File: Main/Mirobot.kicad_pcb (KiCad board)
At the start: 2 copper layers, 110 x 31.2 mm, 20 parts, among them IC1 ARDUINO_PRO_MINI, M1 ESP8266-ESP-07, P3 RIGHT_STEPPER, P4 LEFT_STEPPER, SW1 POWER_SWITCH, SW2 LEFT_BUMP, SW3 RIGHT_BUMP, U2 ULN2803A

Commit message: Updated for version 2.0f
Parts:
- added P1: CONN_01X02, Mirobot:2-PIN-EDGE-CONN, B.Cu at (201.8, 105.9)
- LINE1: moved to B.Cu
- M1: value ESP8266-ESP-07 -> ESP8266-ESP-12
- R1, R2, R3: footprint Resistors_SMD:R_0603_HandSoldering -> Mirobot:R_0603_HandSoldering_Universal_TH
- moved R2 3.30 mm to (161.8, 129.7), turned to 90 degrees
- moved PEN1 2.54 mm to (132.5, 130.6), turned to 270 degrees
- moved R3 2.16 mm to (170.8, 120.8)
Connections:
- M1 pad 11: (no net) -> Net-(M1-Pad11)
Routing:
- net Net-(M1-Pad11): track 0.00 -> 32.7 mm, vias 0 -> 2
- net GND: track 40.0 -> 63.7 mm, vias 9 -> 17
- net Net-(M1-Pad10): track 3.54 -> 8.30 mm
- net Net-(IC1-Pad17): track 41.8 -> 44.9 mm
- net +3V3: track 96.1 -> 93.7 mm
- net Net-(IC1-Pad18): track 45.7 -> 47.7 mm
- net Net-(IC1-Pad16): track 38.1 -> 40.0 mm, vias 2 -> 1
- net Net-(M1-Pad1): track 11.4 -> 12.5 mm
- net Net-(IC1-Pad12): track 55.3 -> 55.9 mm
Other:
- board text added: "POWER"
- board text added: "v2.0f"
- board text removed: "v2.0d"

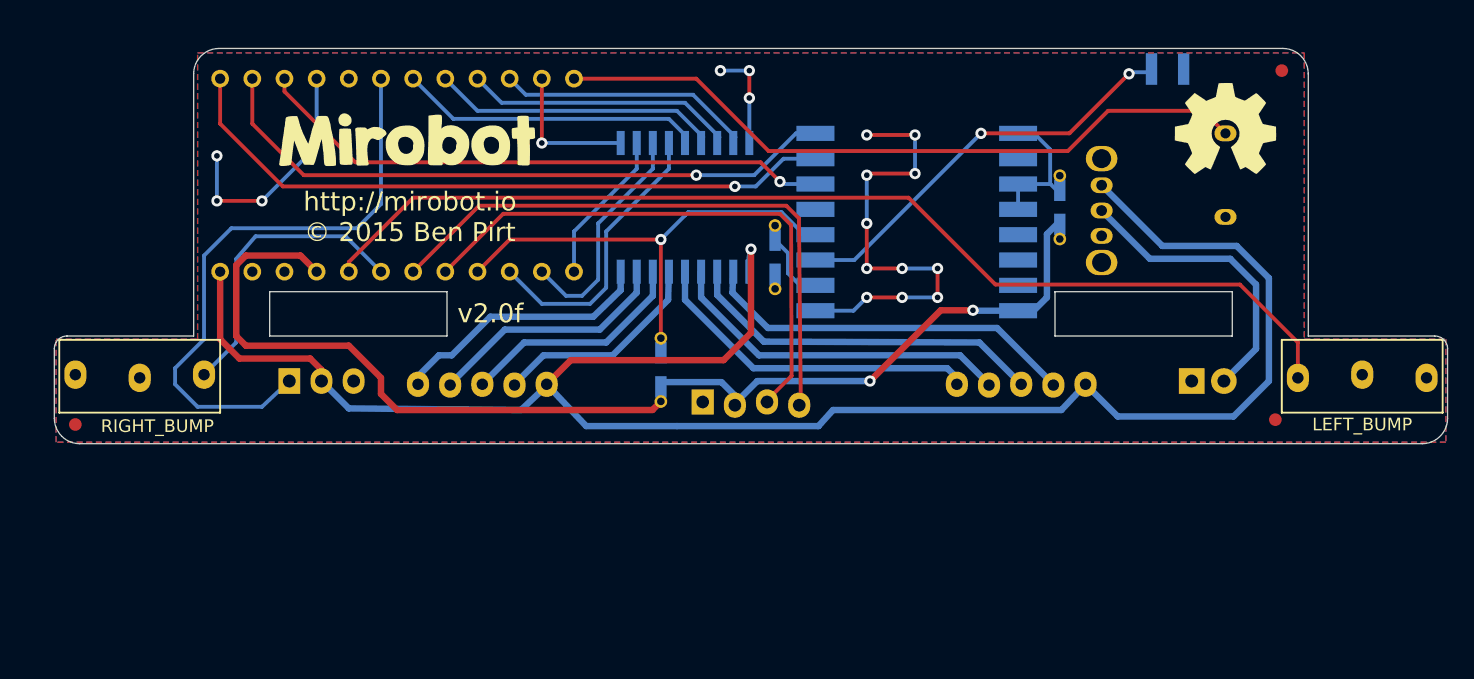
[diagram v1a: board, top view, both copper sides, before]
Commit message: Use a different pin for bringing GPIO0 out
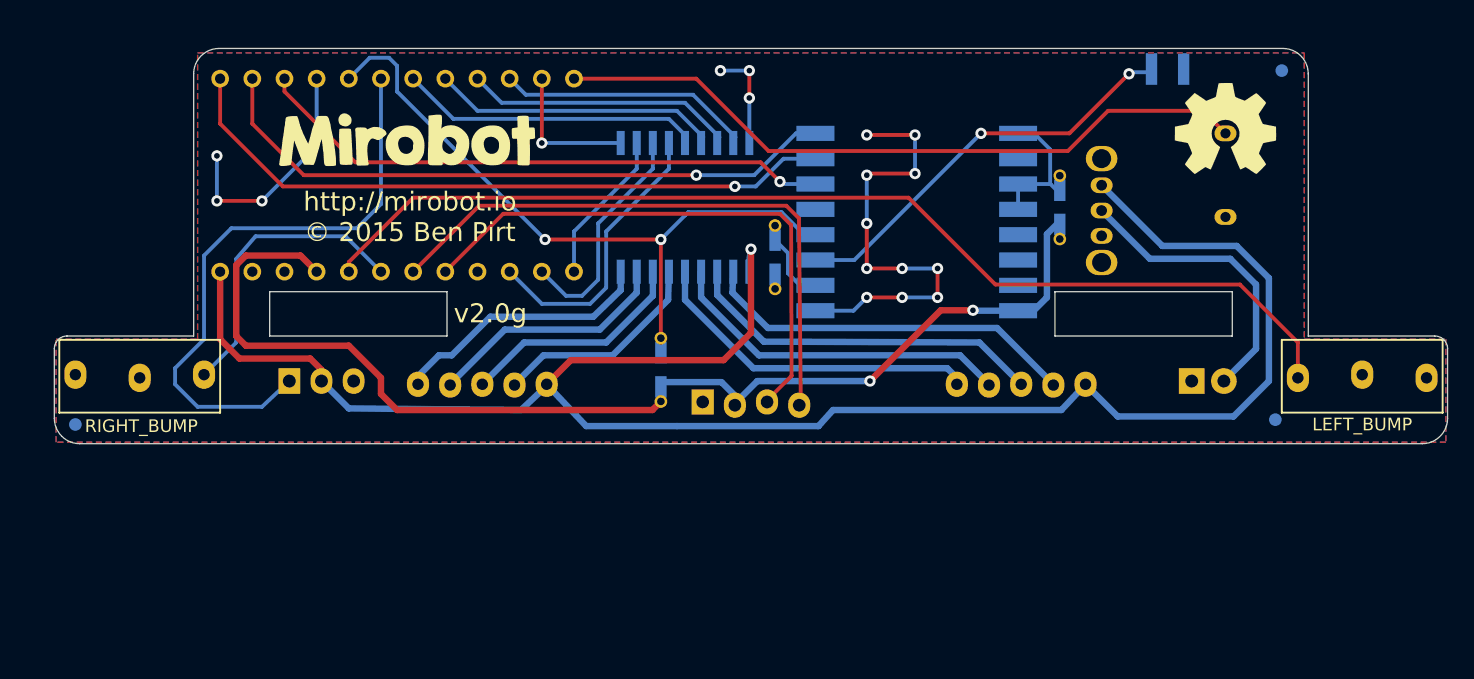
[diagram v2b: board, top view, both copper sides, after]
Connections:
- IC1 pad 16: Net-(IC1-Pad16) -> (no net)
- IC1 pad 5: (no net) -> Net-(IC1-Pad5)
- M1 pad 12: Net-(IC1-Pad16) -> Net-(IC1-Pad5)
- R2 pad 2: Net-(IC1-Pad16) -> Net-(IC1-Pad5)
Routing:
- net Net-(IC1-Pad5): track 0.00 -> 56.9 mm, vias 0 -> 2
- net Net-(IC1-Pad16): track 40.0 -> 0.00 mm, vias 1 -> 0
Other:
- board text added: "v2.0g"
- board text removed: "v2.0f"
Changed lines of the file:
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@@
     (thickness 1.6)
     (drawings 37)
-    (tracks 271)
+    (tracks 276)
     (zones 0)
     (modules 21)
@@
     (mod_text_size 1 1)
     (mod_text_width 0.15)
-    (pad_size 0.9 2.5)
+    (pad_size 1 1)
     (pad_drill 0)
     (pad_to_mask_clearance 0)
@@
   (net 30 "Net-(M1-Pad1)")
   (net 31 "Net-(M1-Pad10)")
-  (net 32 "Net-(IC1-Pad16)")
-  (net 33 "Net-(M1-Pad11)")
+  (net 32 "Net-(M1-Pad11)")
+  (net 33 "Net-(IC1-Pad5)")
   (net_class Default "This is the default net class."
     (clearance 0.254)
@@
     (add_net "Net-(IC1-Pad14)")
     (add_net "Net-(IC1-Pad15)")
-    (add_net "Net-(IC1-Pad16)")
     (add_net "Net-(IC1-Pad17)")
     (add_net "Net-(IC1-Pad18)")
@@
     (add_net "Net-(IC1-Pad20)")
     (add_net "Net-(IC1-Pad3)")
+    (add_net "Net-(IC1-Pad5)")
     (add_net "Net-(IC1-Pad6)")
     (add_net "Net-(IC1-Pad7)")
@@
       (effects (font (size 1 1) (thickness 0.15)))
     )
-    (pad 1 smd circle (at 0 0) (size 1 1) (layers F.Cu F.Mask)
+    (pad 1 smd circle (at 0 0) (size 1 1) (layers B.Cu B.Mask)
       (solder_mask_margin 1) (clearance 1))
   )
@@
       (effects (font (size 1 1) (thickness 0.15)))
     )
-    (pad 1 smd circle (at 0 0) (size 1 1) (layers F.Cu F.Mask)
+    (pad 1 smd circle (at 0 0) (size 1 1) (layers B.Cu B.Mask)
       (solder_mask_margin 1) (clearance 1))
   )
@@
       (effects (font (size 1 1) (thickness 0.15)))
     )
-    (pad 1 smd circle (at 0 0) (size 1 1) (layers F.Cu F.Mask)
+    (pad 1 smd circle (at 0 0) (size 1 1) (layers B.Cu B.Mask)
       (solder_mask_margin 1) (clearance 1))
   )
@@
     (pad 4 thru_hole circle (at -6.35 -7.62) (size 1.397 1.397) (drill 0.8128) (layers *.Cu *.Mask B.SilkS)
       (net 4 GND))
-    (pad 5 thru_hole circle (at -3.81 -7.62) (size 1.397 1.397) (drill 0.8128) (layers *.Cu *.Mask B.SilkS))
+    (pad 5 thru_hole circle (at -3.81 -7.62) (size 1.397 1.397) (drill 0.8128) (layers *.Cu *.Mask B.SilkS)
+      (net 33 "Net-(IC1-Pad5)"))
     (pad 6 thru_hole circle (at -1.27 -7.62) (size 1.397 1.397) (drill 0.8128) (layers *.Cu *.Mask B.SilkS)
       (net 5 "Net-(IC1-Pad6)"))
@@
     (pad 15 thru_hole circle (at 8.89 7.62) (size 1.397 1.397) (drill 0.8128) (layers *.Cu *.Mask B.SilkS)
       (net 14 "Net-(IC1-Pad15)"))
-    (pad 16 thru_hole circle (at 6.35 7.62) (size 1.397 1.397) (drill 0.8128) (layers *.Cu *.Mask B.SilkS)
-      (net 32 "Net-(IC1-Pad16)"))
+    (pad 16 thru_hole circle (at 6.35 7.62) (size 1.397 1.397) (drill 0.8128) (layers *.Cu *.Mask B.SilkS))
     (pad 17 thru_hole circle (at 3.81 7.62) (size 1.397 1.397) (drill 0.8128) (layers *.Cu *.Mask B.SilkS)
       (net 15 "Net-(IC1-Pad17)"))
@@
       (effects (font (size 1 1) (thickness 0.15)))
     )
-    (fp_text value RIGHT_BUMP (at -1.397 -3.937 180) (layer F.SilkS)
+    (fp_text value RIGHT_BUMP (at -0.127 -3.937 180) (layer F.SilkS)
       (effects (font (size 1 1) (thickness 0.15)))
     )
@@
       (net 19 +3V3))
     (pad 2 smd rect (at 1.35 0 90) (size 1.7 0.9) (layers B.Cu B.Paste B.Mask)
-      (net 32 "Net-(IC1-Pad16)"))
+      (net 33 "Net-(IC1-Pad5)"))
     (pad 1 thru_hole circle (at -2.5 0 90) (size 1 1) (drill 0.6) (layers *.Cu *.Mask B.SilkS)
       (net 19 +3V3))
     (pad 2 thru_hole circle (at 2.5 0 90) (size 1 1) (drill 0.6) (layers *.Cu *.Mask B.SilkS)
-      (net 32 "Net-(IC1-Pad16)"))
+      (net 33 "Net-(IC1-Pad5)"))
     (model Resistors_SMD.3dshapes/R_0603_HandSoldering.wrl
       (at (xyz 0 0 0))
@@
       (net 4 GND))
     (pad 1 smd rect (at -1.27 0) (size 0.9 2.5) (layers B.Cu B.Paste B.Mask)
-      (net 33 "Net-(M1-Pad11)"))
+      (net 32 "Net-(M1-Pad11)"))
   )
   (module Mirobot:ESP-07 (layer B.Cu)
@@
       (net 31 "Net-(M1-Pad10)"))
     (pad 12 smd rect (at 2 8 270) (size 1.2 3) (layers B.Cu B.Paste B.Mask)
-      (net 32 "Net-(IC1-Pad16)"))
+      (net 33 "Net-(IC1-Pad5)"))
     (pad 13 smd rect (at 0 8 270) (size 1.2 3) (layers B.Cu B.Paste B.Mask))
     (pad 14 smd rect (at -2 8 270) (size 1.2 3) (layers B.Cu B.Paste B.Mask)
@@
       (net 2 "Net-(IC1-Pad2)"))
     (pad 11 smd rect (at 4 8 270) (size 1.2 3) (layers B.Cu B.Paste B.Mask)
-      (net 33 "Net-(M1-Pad11)"))
+      (net 32 "Net-(M1-Pad11)"))
   )
   (module Mirobot:JST_XH-1x05 (layer B.Cu)
@@
     (effects (font (size 1.5 1.5) (thickness 0.3)))
   )
-  (gr_text v2.0f (at 148.336 125.222) (layer F.SilkS)
+  (gr_text v2.0g (at 148.336 125.222) (layer F.SilkS)
     (effects (font (size 1.5 1.5) (thickness 0.3)))
   )
@@
   (segment (start 173.165 123) (end 174 123) (width 0.3048) (layer B.Cu) (net 31) (status 30))
   (segment (start 173.292 123) (end 174 123) (width 0.3048) (layer B.Cu) (net 31) (status 30))
-  (segment (start 161.798 127.167) (end 161.798 128.317) (width 0.3048) (layer B.Cu) (net 32))
-  (segment (start 163.703 117.475) (end 163.957 117.221) (width 0.3048) (layer B.Cu) (net 32))
-  (segment (start 161.798 119.38) (end 163.703 117.475) (width 0.3048) (layer B.Cu) (net 32))
-  (via (at 161.798 119.38) (size 0.889) (layers F.Cu B.Cu) (net 32))
-  (segment (start 171.323 117.221) (end 173.102 119) (width 0.3048) (layer B.Cu) (net 32))
-  (segment (start 163.957 117.221) (end 171.323 117.221) (width 0.3048) (layer B.Cu) (net 32))
-  (segment (start 173.102 119) (end 174 119) (width 0.3048) (layer B.Cu) (net 32))
-  (segment (start 161.798 127.54) (end 161.798 119.38) (width 0.3048) (layer F.Cu) (net 32) (status 10))
-  (segment (start 172.721 119) (end 174 119) (width 0.3048) (layer B.Cu) (net 32) (status 30))
-  (segment (start 149.86 119.38) (end 147.32 121.92) (width 0.3048) (layer F.Cu) (net 32) (status 20))
-  (segment (start 161.798 119.38) (end 149.86 119.38) (width 0.3048) (layer F.Cu) (net 32))
-  (segment (start 174 121) (end 177.069 121) (width 0.3048) (layer B.Cu) (net 33))
-  (segment (start 198.882 106.172) (end 200.533 106.172) (width 0.3048) (layer B.Cu) (net 33))
-  (segment (start 198.755 106.299) (end 198.882 106.172) (width 0.3048) (layer B.Cu) (net 33))
-  (via (at 198.755 106.299) (size 0.889) (layers F.Cu B.Cu) (net 33))
-  (segment (start 194.056 110.998) (end 198.755 106.299) (width 0.3048) (layer F.Cu) (net 33))
-  (segment (start 187.071 110.998) (end 194.056 110.998) (width 0.3048) (layer F.Cu) (net 33))
-  (via (at 187.071 110.998) (size 0.889) (layers F.Cu B.Cu) (net 33))
-  (segment (start 177.069 121) (end 187.071 110.998) (width 0.3048) (layer B.Cu) (net 33))
+  (segment (start 174 121) (end 177.069 121) (width 0.3048) (layer B.Cu) (net 32))
+  (segment (start 198.882 106.172) (end 200.533 106.172) (width 0.3048) (layer B.Cu) (net 32))
+  (segment (start 198.755 106.299) (end 198.882 106.172) (width 0.3048) (layer B.Cu) (net 32))
+  (via (at 198.755 106.299) (size 0.889) (layers F.Cu B.Cu) (net 32))
+  (segment (start 194.056 110.998) (end 198.755 106.299) (width 0.3048) (layer F.Cu) (net 32))
+  (segment (start 187.071 110.998) (end 194.056 110.998) (width 0.3048) (layer F.Cu) (net 32))
+  (via (at 187.071 110.998) (size 0.889) (layers F.Cu B.Cu) (net 32))
+  (segment (start 177.069 121) (end 187.071 110.998) (width 0.3048) (layer B.Cu) (net 32))
+  (segment (start 161.798 127.167) (end 161.798 128.317) (width 0.3048) (layer B.Cu) (net 33))
+  (segment (start 163.703 117.475) (end 163.957 117.221) (width 0.3048) (layer B.Cu) (net 33))
+  (segment (start 161.798 119.38) (end 163.703 117.475) (width 0.3048) (layer B.Cu) (net 33))
+  (via (at 161.798 119.38) (size 0.889) (layers F.Cu B.Cu) (net 33))
+  (segment (start 171.323 117.221) (end 173.102 119) (width 0.3048) (layer B.Cu) (net 33))
+  (segment (start 163.957 117.221) (end 171.323 117.221) (width 0.3048) (layer B.Cu) (net 33))
+  (segment (start 173.102 119) (end 174 119) (width 0.3048) (layer B.Cu) (net 33))
+  (segment (start 161.798 127.54) (end 161.798 119.38) (width 0.3048) (layer F.Cu) (net 33) (status 10))
+  (segment (start 172.721 119) (end 174 119) (width 0.3048) (layer B.Cu) (net 33) (status 30))
+  (segment (start 161.798 119.38) (end 152.654 119.38) (width 0.3048) (layer F.Cu) (net 33))
+  (segment (start 138.811 105.029) (end 140.335 105.029) (width 0.3048) (layer B.Cu) (net 33))
+  (segment (start 140.335 105.029) (end 140.97 105.664) (width 0.3048) (layer B.Cu) (net 33))
+  (segment (start 140.97 105.664) (end 140.97 107.696) (width 0.3048) (layer B.Cu) (net 33))
+  (segment (start 140.97 107.696) (end 152.654 119.38) (width 0.3048) (layer B.Cu) (net 33))
+  (via (at 152.654 119.38) (size 0.889) (layers F.Cu B.Cu) (net 33))
+  (segment (start 137.16 106.68) (end 138.811 105.029) (width 0.3048) (layer B.Cu) (net 33))
   (zone (net 4) (net_name GND) (layer F.Cu) (hatch edge 0.508)
     (connect_pads (clearance 0.508))

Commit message: Improve power handling
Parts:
- added C1: 470uF, Capacitors_SMD:c_elec_6.3x7.7, B.Cu at (207.6, 119.8)
- added C2: 470uF, Capacitors_SMD:c_elec_6.3x7.7, B.Cu at (134.6, 114.5)
- added C3: 100uF, Capacitors_Tantalum_SMD:TantalC_SizeB_EIA-3528_Reflow, B.Cu at (178.5, 131.8)
- PEN1: footprint Pin_Headers:Pin_Header_Straight_1x03 -> Mirobot:Pin_Header_Staggered_1x03
- R1, R2, R3: footprint Mirobot:R_0603_HandSoldering_Universal_TH -> Resistors_SMD:R_0603
- moved P1 4.80 mm to (197.0, 106.1)
- moved SG1 4.17 mm to (206.5, 110.1)
- moved R1 3.56 mm to (193.1, 120.4)
- moved PEN1 2.54 mm to (135.0, 130.4), turned to 0 degrees
- moved ART2 2.42 mm to (206.5, 113.0)
- moved R3 1.32 mm to (171.0, 122.1)
- moved SW1 1.13 mm to (197.5, 116.5)
- moved R2 0.20 mm to (161.8, 129.9)
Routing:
- net VSS: track 147.5 -> 206.0 mm
- net +3V3: track 93.7 -> 107.6 mm, vias 2 -> 4
- net Net-(IC1-Pad19): track 23.7 -> 33.1 mm, vias 0 -> 1
- net Net-(IC1-Pad5): track 56.9 -> 60.9 mm, vias 2 -> 4
- net Net-(M1-Pad11): track 32.7 -> 29.8 mm
- net GND: track 63.7 -> 66.1 mm, vias 17 -> 19
- net Net-(M1-Pad1): track 12.5 -> 14.6 mm
- net Net-(M1-Pad10): track 8.30 -> 6.41 mm
- net Net-(IC1-Pad18): track 47.7 -> 45.8 mm
- net Net-(IC1-Pad17): track 44.9 -> 43.3 mm
- net Net-(IC1-Pad6): track 47.2 -> 45.8 mm
- net Net-(IC1-Pad1): track 53.8 -> 53.1 mm
- net Net-(IC1-Pad2): track 51.1 -> 50.5 mm
- net Net-(IC1-Pad20): track 85.2 -> 85.8 mm
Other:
- net class High Power added: clearance 0.254, trace_width 0.7, via_dia 0.889, via_drill 0.635
- board text added: "The module above is based on the Pro Mini by Sparkfun"
- board text added: "v2.1"
- board text removed: "The module above is based on the Pro Mini by Sparkfun sparkfun.com/products/11114"
- board text removed: "v2.0g"

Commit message: initial version of v3.0
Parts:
- removed IC1: ARDUINO_PRO_MINI, Mirobot:ARDUINO_PRO_MINI
- removed LINE1: LINE, Mirobot:Pin_Header_Staggered_1x04
- removed P1: CONN_01X02, Mirobot:2-PIN-EDGE-CONN
- removed P4: LEFT_STEPPER, Mirobot:JST_XH-1x05
- added C6: 10uF, Capacitors_SMD:C_0805, B.Cu at (212.7, 137.0)
- added C7: 100uF, Capacitors_Tantalum_SMD:TantalC_SizeB_EIA-3528_Reflow, B.Cu at (175.8, 145.9)
- added C8: 10uF, Capacitors_SMD:C_0805, B.Cu at (212.7, 141.4)
- added D1: LED, Mirobot:SIDE-LED-REVERSED, B.Cu at (150.9, 149.4)
- added D2: LED, Mirobot:SIDE-LED-REVERSED, B.Cu at (186.9, 149.4)
- added L1: WS2812B, Mirobot:WS2812B, B.Cu at (157.2, 124.2)
- added P2: RIGHT_STEPPER, Mirobot:JST_XH-1x05, B.Cu at (193.3, 130.9)
- added Q1: S8050, TO_SOT_Packages_SMD:SOT-23, B.Cu at (130.4, 136.4)
- added Q2: S8050, TO_SOT_Packages_SMD:SOT-23, B.Cu at (130.4, 142.5)
- added R10: 10k, Resistors_SMD:R_0603, B.Cu at (129.5, 139.4)
- added R11: 10k, Resistors_SMD:R_0603, B.Cu at (131.3, 139.4)
- added R4: 10k, Resistors_SMD:R_0603, B.Cu at (167.9, 145.4)
- added R5: 10k, Resistors_SMD:R_0603, B.Cu at (166.0, 145.4)
- added R6: 20k, Resistors_SMD:R_0603, B.Cu at (169.8, 145.4)
- added R7: 160R, Resistors_SMD:R_0603, B.Cu at (162.2, 145.4)
- added R8: 20k, Resistors_SMD:R_0603, B.Cu at (164.1, 145.4)
- added R9: 160R, Resistors_SMD:R_0603, B.Cu at (171.7, 145.4)
- added U1: phototransistor, Mirobot:SIDE-LED, B.Cu at (178.9, 150.0)
- added U3: PCF8591, SMD_Packages:SO-16-L, B.Cu at (152.5, 140.5)
- added U4: 74HC595, SMD_Packages:SO-16-N, B.Cu at (184.2, 140.0)
- added U5: ULN2803A, Mirobot:SO-18, B.Cu at (194.7, 140.6)
- added U6: USB-A-PLUG, Connect:USB_Micro-B, B.Cu at (149.6, 124.5)
- added U7: CH340G, SMD_Packages:SO-16-N, B.Cu at (123.8, 139.7)
- added U8: LD1117S33CTR, TO_SOT_Packages_SMD:SOT-223, B.Cu at (218.8, 139.7)
- added X1: 12MHz, Crystals:crystal_FA238-TSX3225, B.Cu at (117.2, 138.6)
- C1, C2: value 470uF -> 22pF; footprint Capacitors_SMD:c_elec_6.3x7.7 -> Capacitors_SMD:C_0805
- C3: value 100uF -> 470uF; footprint Capacitors_Tantalum_SMD:TantalC_SizeB_EIA-3528_Reflow -> Capacitors_SMD:c_elec_8x10
- P3: value RIGHT_STEPPER -> LEFT_STEPPER
- SW1: value POWER_SWITCH -> LEFT_BUMP; footprint Mirobot:SMALL_SLIDE_SWITCH -> Mirobot:LEVER_SWITCH; moved to F.Cu
- SW2: value LEFT_BUMP -> RIGHT_BUMP
- SW3: value RIGHT_BUMP -> POWER_SWITCH; footprint Mirobot:LEVER_SWITCH -> Mirobot:SMALL_SLIDE_SWITCH; moved to B.Cu
- U2: value ULN2803A -> phototransistor; footprint Mirobot:SO-18 -> Mirobot:SIDE-LED
- moved C1 93.0 mm to (117.2, 141.6)
- moved SW1 78.1 mm to (120.7, 130.2), turned to 180 degrees
- moved SG1 73.7 mm to (139.3, 140.5)
- moved SW3 65.6 mm to (185.9, 123.3)
- moved FID3 38.6 mm to (209.9, 144.7)
- moved U2 33.4 mm to (158.9, 150.0), turned to 270 degrees
- moved ART1 29.4 mm to (126.1, 136.4)
- moved C3 29.2 mm to (206.5, 140.0), turned to 90 degrees
- moved ART2 28.4 mm to (217.3, 139.3)
- moved C2 27.3 mm to (117.2, 135.5), turned to 0 degrees
- moved R3 25.7 mm to (160.3, 145.4)
- moved M1 20.5 mm to (170.2, 133.7)
- moved R2 20.1 mm to (181.9, 129.0), turned to 270 degrees
- moved FID1 16.3 mm to (128.0, 123.4)
- moved R1 16.3 mm to (181.9, 132.2), turned to 90 degrees
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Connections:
- C1 pad 1: VSS -> Net-(C1-Pad1)
- C2 pad 1: +3V3 -> Net-(C2-Pad1)
- C3 pad 1: +3V3 -> VSS
- M1 pad 1: Net-(M1-Pad1) -> RESET
- M1 pad 10: Net-(M1-Pad10) -> SERVO
- M1 pad 11: Net-(M1-Pad11) -> SDA
- M1 pad 12: Net-(IC1-Pad5) -> SCL
- M1 pad 13: (no net) -> LED
- M1 pad 14: Net-(IC1-Pad3) -> GPIO5
- M1 pad 15: Net-(IC1-Pad1) -> RXD
- M1 pad 16: Net-(IC1-Pad2) -> TXD
- M1 pad 2: (no net) -> ADC
- M1 pad 3: Net-(M1-Pad1) -> CH_PD
- M1 pad 4: Net-(M1-Pad1) -> BUZZER
- M1 pad 5: (no net) -> SR_LATCH
- M1 pad 6: (no net) -> SR_DATA
- M1 pad 7: (no net) -> SR_CLK
- PEN1 pad 1: Net-(IC1-Pad6) -> SERVO
- R1 pad 1: Net-(M1-Pad1) -> CH_PD
- R2 pad 1: +3V3 -> RESET
- R2 pad 2: Net-(IC1-Pad5) -> +3V3
- R3 pad 2: Net-(M1-Pad10) -> SERVO
- SG1 pad 1: Net-(IC1-Pad12) -> BUZZER
- SW1 pad 1: VSS -> +3V3
- SW1 pad 2: Net-(BATT1-Pad2) -> Net-(SW1-Pad2)
- SW1 pad 3: (no net) -> GND
- SW2 pad 1: GND -> +3V3
- SW2 pad 3: (no net) -> GND
- SW3 pad 1: GND -> VSS
- SW3 pad 2: Net-(IC1-Pad19) -> Net-(BATT1-Pad2)
- SW3 pad 3: (no net) -> Net-(SW3-Pad3)
- U2 pad 2: Net-(IC1-Pad13) -> GND
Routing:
- net +3V3: track 107.6 -> 191.6 mm
- net VSS: track 206.0 -> 132.6 mm, vias 1 -> 0
- net RESET: track 0.00 -> 60.9 mm, vias 0 -> 2
- net Net-(IC1-Pad5): track 60.9 -> 0.00 mm, vias 4 -> 0
- net Net-(IC1-Pad12): track 56.2 -> 0.00 mm
- net Net-(IC1-Pad1): track 53.1 -> 0.00 mm, vias 1 -> 0
- net Net-(IC1-Pad2): track 50.5 -> 0.00 mm, vias 1 -> 0
- net RXD: track 0.00 -> 47.9 mm, vias 0 -> 2
- net SCL: track 0.00 -> 47.8 mm
- net TXD: track 0.00 -> 47.3 mm, vias 0 -> 2
- net Net-(IC1-Pad3): track 46.0 -> 0.00 mm, vias 1 -> 0
- net Net-(IC1-Pad18): track 45.8 -> 0.00 mm
- net Net-(IC1-Pad6): track 45.8 -> 0.00 mm
- net Net-(IC1-Pad17): track 43.3 -> 0.00 mm
- net SERVO: track 0.00 -> 42.0 mm, vias 0 -> 1
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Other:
- board size 110 x 31.2 mm -> 110 x 31.5 mm
- board text added: "v3.0"
- board text removed: "GND"
- board text removed: "LINE"
- board text removed: "The module above is based on the Pro Mini by Sparkfun"
- board text removed: "v2.1"
